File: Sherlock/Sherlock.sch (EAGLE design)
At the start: 24 parts, among them U3 XBEE-1B2, X1 2540-

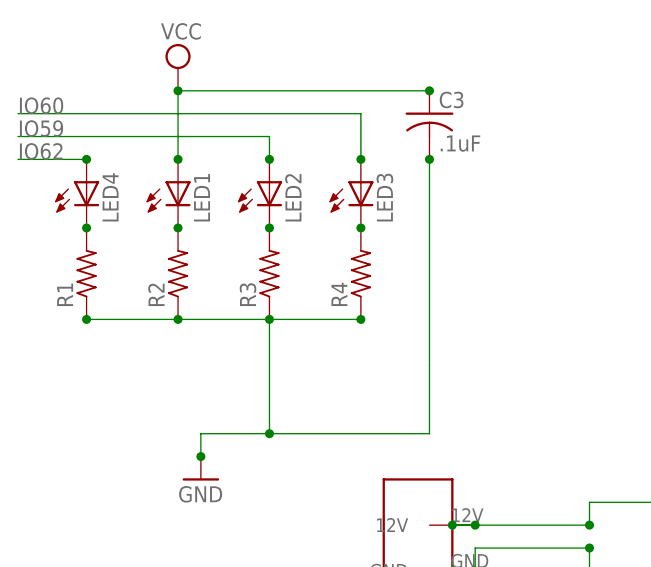
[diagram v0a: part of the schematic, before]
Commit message: Added resistor values for R1-R4 for Sherlock
Change-Id: Ic35e8ce0279ecb8ac04751f8d59191d34fd62b27
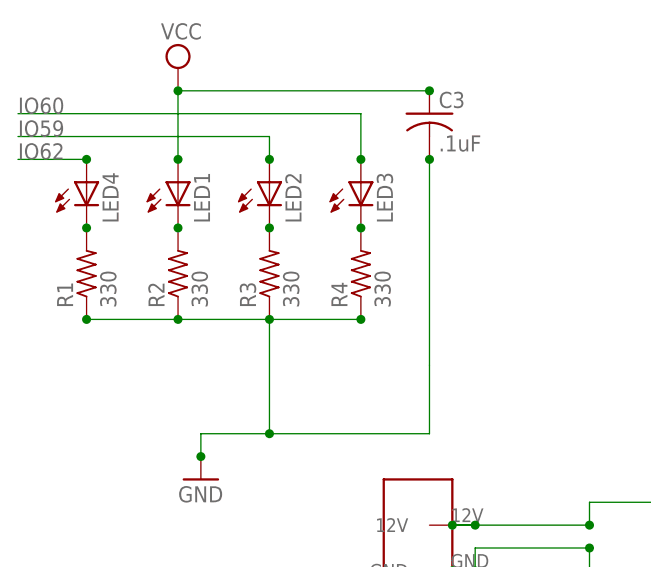
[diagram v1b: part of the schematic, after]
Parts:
- R1, R2, R3, R4: value (none) -> 330
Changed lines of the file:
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@@
 <?xml version="1.0" encoding="utf-8"?>
 <!DOCTYPE eagle SYSTEM "eagle.dtd">
-<eagle version="6.2">
+<eagle version="6.3">
 <drawing>
 <settings>
@@
 <grid distance="0.1" unitdist="inch" unit="inch" style="lines" multiple="1" display="no" altdistance="0.01" altunitdist="inch" altunit="inch"/>
 <layers>
-<layer number="1" name="Top" color="4" fill="1" visible="yes" active="no"/>
-<layer number="2" name="Route2" color="1" fill="3" visible="yes" active="no"/>
-<layer number="3" name="Route3" color="4" fill="3" visible="yes" active="no"/>
-<layer number="4" name="Route4" color="1" fill="4" visible="yes" active="no"/>
-<layer number="5" name="Route5" color="4" fill="4" visible="yes" active="no"/>
-<layer number="6" name="Route6" color="1" fill="8" visible="yes" active="no"/>
-<layer number="7" name="Route7" color="4" fill="8" visible="yes" active="no"/>
-<layer number="8" name="Route8" color="1" fill="2" visible="yes" active="no"/>
-<layer number="9" name="Route9" color="4" fill="2" visible="yes" active="no"/>
-<layer number="10" name="Route10" color="1" fill="7" visible="yes" active="no"/>
-<layer number="11" name="Route11" color="4" fill="7" visible="yes" active="no"/>
-<layer number="12" name="Route12" color="1" fill="5" visible="yes" active="no"/>
-<layer number="13" name="Route13" color="4" fill="5" visible="yes" active="no"/>
-<layer number="14" name="Route14" color="1" fill="6" visible="yes" active="no"/>
-<layer number="15" name="Route15" color="4" fill="6" visible="yes" active="no"/>
-<layer number="16" name="Bottom" color="1" fill="1" visible="yes" active="no"/>
-<layer number="17" name="Pads" color="2" fill="1" visible="yes" active="no"/>
-<layer number="18" name="Vias" color="2" fill="1" visible="yes" active="no"/>
-<layer number="19" name="Unrouted" color="6" fill="1" visible="yes" active="no"/>
-<layer number="20" name="Dimension" color="15" fill="1" visible="yes" active="no"/>
-<layer number="21" name="tPlace" color="7" fill="1" visible="yes" active="no"/>
-<layer number="22" name="bPlace" color="7" fill="1" visible="yes" active="no"/>
-<layer number="23" name="tOrigins" color="15" fill="1" visible="yes" active="no"/>
-<layer number="24" name="bOrigins" color="15" fill="1" visible="yes" active="no"/>
-<layer number="25" name="tNames" color="7" fill="1" visible="yes" active="no"/>
-<layer number="26" name="bNames" color="7" fill="1" visible="yes" active="no"/>
-<layer number="27" name="tValues" color="7" fill="1" visible="yes" active="no"/>
-<layer number="28" name="bValues" color="7" fill="1" visible="yes" active="no"/>
+<layer number="1" name="Top" color="4" fill="1" visible="no" active="no"/>
+<layer number="2" name="Route2" color="1" fill="3" visible="no" active="no"/>
+<layer number="3" name="Route3" color="4" fill="3" visible="no" active="no"/>
+<layer number="4" name="Route4" color="1" fill="4" visible="no" active="no"/>
+<layer number="5" name="Route5" color="4" fill="4" visible="no" active="no"/>
+<layer number="6" name="Route6" color="1" fill="8" visible="no" active="no"/>
+<layer number="7" name="Route7" color="4" fill="8" visible="no" active="no"/>
+<layer number="8" name="Route8" color="1" fill="2" visible="no" active="no"/>
+<layer number="9" name="Route9" color="4" fill="2" visible="no" active="no"/>
+<layer number="10" name="Route10" color="1" fill="7" visible="no" active="no"/>
+<layer number="11" name="Route11" color="4" fill="7" visible="no" active="no"/>
+<layer number="12" name="Route12" color="1" fill="5" visible="no" active="no"/>
+<layer number="13" name="Route13" color="4" fill="5" visible="no" active="no"/>
+<layer number="14" name="Route14" color="1" fill="6" visible="no" active="no"/>
+<layer number="15" name="Route15" color="4" fill="6" visible="no" active="no"/>
+<layer number="16" name="Bottom" color="1" fill="1" visible="no" active="no"/>
+<layer number="17" name="Pads" color="2" fill="1" visible="no" active="no"/>
+<layer number="18" name="Vias" color="2" fill="1" visible="no" active="no"/>
+<layer number="19" name="Unrouted" color="6" fill="1" visible="no" active="no"/>
+<layer number="20" name="Dimension" color="15" fill="1" visible="no" active="no"/>
+<layer number="21" name="tPlace" color="7" fill="1" visible="no" active="no"/>
+<layer number="22" name="bPlace" color="7" fill="1" visible="no" active="no"/>
+<layer number="23" name="tOrigins" color="15" fill="1" visible="no" active="no"/>
+<layer number="24" name="bOrigins" color="15" fill="1" visible="no" active="no"/>
+<layer number="25" name="tNames" color="7" fill="1" visible="no" active="no"/>
+<layer number="26" name="bNames" color="7" fill="1" visible="no" active="no"/>
+<layer number="27" name="tValues" color="7" fill="1" visible="no" active="no"/>
+<layer number="28" name="bValues" color="7" fill="1" visible="no" active="no"/>
 <layer number="29" name="tStop" color="7" fill="3" visible="no" active="no"/>
 <layer number="30" name="bStop" color="7" fill="6" visible="no" active="no"/>
@@
 <layer number="35" name="tGlue" color="7" fill="4" visible="no" active="no"/>
 <layer number="36" name="bGlue" color="7" fill="5" visible="no" active="no"/>
-<layer number="37" name="tTest" color="7" fill="1" visible="yes" active="no"/>
-<layer number="38" name="bTest" color="7" fill="1" visible="yes" active="no"/>
+<layer number="37" name="tTest" color="7" fill="1" visible="no" active="no"/>
+<layer number="38" name="bTest" color="7" fill="1" visible="no" active="no"/>
 <layer number="39" name="tKeepout" color="4" fill="11" visible="no" active="no"/>
 <layer number="40" name="bKeepout" color="1" fill="11" visible="no" active="no"/>
@@
 <layer number="44" name="Drills" color="7" fill="1" visible="no" active="no"/>
 <layer number="45" name="Holes" color="7" fill="1" visible="no" active="no"/>
-<layer number="46" name="Milling" color="3" fill="1" visible="yes" active="no"/>
-<layer number="47" name="Measures" color="7" fill="1" visible="yes" active="no"/>
-<layer number="48" name="Document" color="7" fill="1" visible="yes" active="no"/>
-<layer number="49" name="Reference" color="7" fill="1" visible="yes" active="no"/>
-<layer number="50" name="dxf" color="7" fill="1" visible="yes" active="no"/>
-<layer number="51" name="tDocu" color="7" fill="1" visible="yes" active="no"/>
-<layer number="52" name="bDocu" color="7" fill="1" visible="yes" active="no"/>
-<layer number="53" name="tGND_GNDA" color="7" fill="9" visible="yes" active="no"/>
-<layer number="54" name="bGND_GNDA" color="1" fill="9" visible="yes" active="no"/>
-<layer number="56" name="wert" color="7" fill="1" visible="yes" active="no"/>
+<layer number="46" name="Milling" color="3" fill="1" visible="no" active="no"/>
+<layer number="47" name="Measures" color="7" fill="1" visible="no" active="no"/>
+<layer number="48" name="Document" color="7" fill="1" visible="no" active="no"/>
+<layer number="49" name="Reference" color="7" fill="1" visible="no" active="no"/>
+<layer number="50" name="dxf" color="7" fill="1" visible="no" active="no"/>
+<layer number="51" name="tDocu" color="7" fill="1" visible="no" active="no"/>
+<layer number="52" name="bDocu" color="7" fill="1" visible="no" active="no"/>
+<layer number="53" name="tGND_GNDA" color="7" fill="9" visible="no" active="no"/>
+<layer number="54" name="bGND_GNDA" color="1" fill="9" visible="no" active="no"/>
+<layer number="56" name="wert" color="7" fill="1" visible="no" active="no"/>
 <layer number="91" name="Nets" color="2" fill="1" visible="yes" active="yes"/>
 <layer number="92" name="Busses" color="1" fill="1" visible="yes" active="yes"/>
@@
 <part name="P3" library="pinhead" deviceset="PINHD-2X20" device=""/>
 <part name="GND3" library="supply1" deviceset="GND" device=""/>
-<part name="R1" library="rcl" deviceset="R-US_" device="R0603"/>
-<part name="R2" library="rcl" deviceset="R-US_" device="R0603"/>
-<part name="R3" library="rcl" deviceset="R-US_" device="R0603"/>
-<part name="R4" library="rcl" deviceset="R-US_" device="R0603"/>
+<part name="R1" library="rcl" deviceset="R-US_" device="R0603" value="330"/>
+<part name="R2" library="rcl" deviceset="R-US_" device="R0603" value="330"/>
+<part name="R3" library="rcl" deviceset="R-US_" device="R0603" value="330"/>
+<part name="R4" library="rcl" deviceset="R-US_" device="R0603" value="330"/>
 <part name="C3" library="rcl" deviceset="C-US" device="C0603K" value=".1uF"/>
 <part name="C1" library="rcl" deviceset="C-US" device="C0603" value=".1uF"/>
